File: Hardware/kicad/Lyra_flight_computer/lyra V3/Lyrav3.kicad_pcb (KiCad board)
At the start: 4 copper layers, 25 x 55 mm, 80 parts, among them J2 Screw_Terminal_01x06, J3 Conn_01x02, J4 Conn_01x02, J5 Conn_01x03, J6 Conn_01x06, J7 USB_B_Micro, J8 Conn_01x04, J9 Screw_Terminal_01x06, Q1 AO3401A, Q2 AO3400A, Q3 AO3400A, Q4 AO3400A, Q5 AO3400A, U1 AZ1117-3.3, U2 BMI088, U3 BMP388, U4 ADXL375BCCZ-RL7, U6 ADS1015IDGS, U8 RP2040, U9 W25Q128JVS, X1 S3D12.288000B20F30T

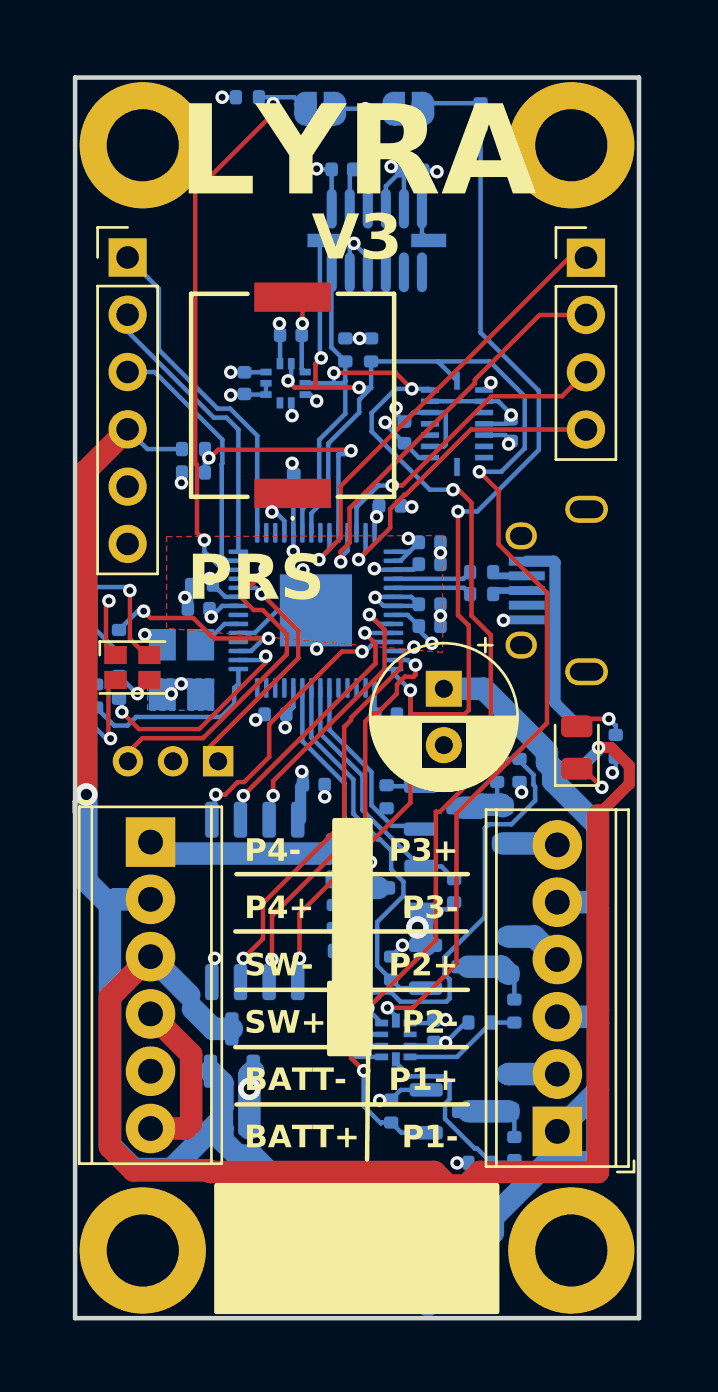
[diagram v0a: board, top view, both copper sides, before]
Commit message: add gps module init
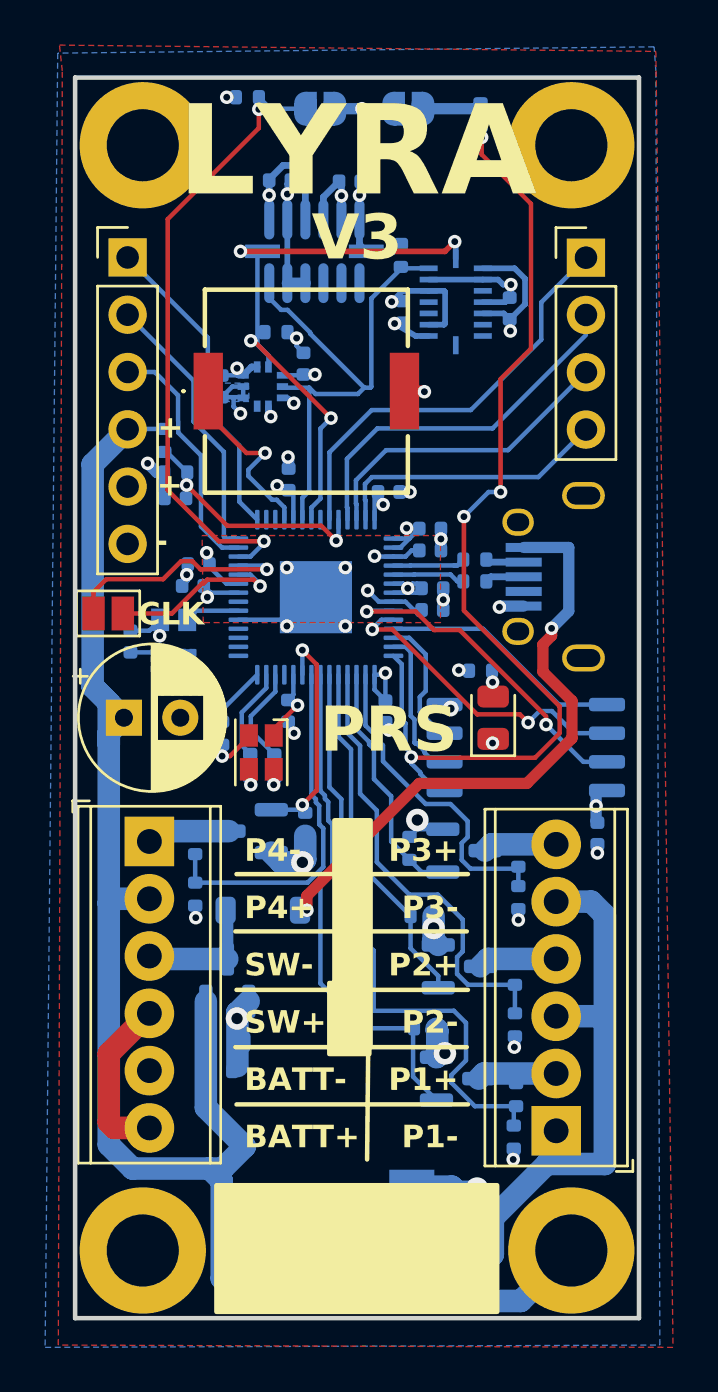
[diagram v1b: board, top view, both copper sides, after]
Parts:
- removed C15: 100n, Capacitor_SMD:C_0402_1005Metric
- removed J5: Conn_01x03, Connector_PinHeader_2.00mm:PinHeader_1x03_P2.00mm_Vertical
- removed R19, R20, R8, R9: 1R, Resistor_SMD:R_0603_1608Metric
- removed U1: AZ1117-3.3, Package_TO_SOT_SMD:SOT-223
- removed U6: ADS1015IDGS, easyeda2kicad:X2QFN-10_L2.0-W1.5-P0.50-BL
- removed X1: S3D12.288000B20F30T, easyeda2kicad:OSC-SMD_4P-L3.2-W2.5-BL_SIT8008BI
- added C13: 100n, Capacitor_SMD:C_0402_1005Metric, B.Cu at (186.1, 89.0)
- added C3: 100n, Capacitor_SMD:C_0402_1005Metric, B.Cu at (188.0, 82.7)
- added J1: Conn_01x02, Jumper:SolderJumper-2_P1.3mm_Open_Pad1.0x1.5mm, F.Cu at (185.1, 87.8)
- added U5: AMS1117-3.3, Package_TO_SOT_SMD:SOT-223-3_TabPin2, B.Cu at (195.4, 115.5)
- added X2: SX1M12.000M10F30TNN, easyeda2kicad:OSC-SMD_4P-L2.0-W1.6-BL, B.Cu at (188.0, 89.0)
- C5, C6, C7: footprint Capacitor_SMD:C_0402_1005Metric -> Capacitor_SMD:C_0603_1608Metric
- D1: footprint Diode_SMD:D_SOD-323 -> Diode_SMD:D_SOD-123
- moved D1 15.7 mm to (191.9, 100.9), turned to 0 degrees
- moved C9 14.2 mm to (185.8, 92.4), turned to 0 degrees
- moved U9 13.8 mm to (203.6, 93.7), turned to 0 degrees
- moved C27 12.8 mm to (206.8, 97.5), turned to -90 degrees
- moved R28 8.82 mm to (192.4, 94.5)
- moved R27 7.23 mm to (193.8, 97.1)
- moved R25 7.11 mm to (188.9, 100.2), turned to -90 degrees
- moved Q5 7.09 mm to (191.4, 97.4)
- moved R23 6.97 mm to (188.9, 97.9)
- moved R3 6.87 mm to (201.6, 90.3), turned to 180 degrees
- moved D4 6.84 mm to (191.9, 93.9), turned to -90 degrees
- moved R22 6.77 mm to (191.4, 94.5), turned to -90 degrees
- moved R2 5.83 mm to (190.1, 93.1), turned to -90 degrees
- moved R13 5.64 mm to (203.3, 100.4)
- moved C2 5.39 mm to (202.9, 74.3)
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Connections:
- Q2 pad 3: Net-(Q2-D) -> /P2-
- Q3 pad 3: Net-(Q3-D) -> /P1-
- Q4 pad 3: Net-(Q4-D) -> /P3-
- Q5 pad 3: Net-(Q5-D) -> /P4-
- R10 pad 1: Net-(Q3-D) -> /P1-
- R11 pad 1: Net-(Q4-D) -> /P3-
- R21 pad 1: Net-(Q2-D) -> /P2-
- R23 pad 1: Net-(Q5-D) -> /P4-
- U8 pad 12: unconnected-(U8-GPIO9-Pad12) -> /LEDBLUE
- U8 pad 13: unconnected-(U8-GPIO10-Pad13) -> /LEDGREEN
- U8 pad 14: unconnected-(U8-GPIO11-Pad14) -> /LEDRED
- U8 pad 15: /LEDRED -> unconnected-(U8-GPIO12-Pad15)
- U8 pad 16: /LEDGREEN -> unconnected-(U8-GPIO13-Pad16)
- U8 pad 17: /LEDBLUE -> unconnected-(U8-GPIO14-Pad17)
- U8 pad 2: unconnected-(U8-GPIO0-Pad2) -> /P3 CONT 
- U8 pad 3: unconnected-(U8-GPIO1-Pad3) -> /P3 EN 
- U8 pad 4: unconnected-(U8-GPIO2-Pad4) -> /P2 CONT 
- U8 pad 5: unconnected-(U8-GPIO3-Pad5) -> /P2 EN 
- U8 pad 6: /P3 EN  -> /P1 CONT 
- U8 pad 7: /P4 EN  -> /P1 EN 
- U8 pad 8: /P2 EN  -> /P4 CONT 
- U8 pad 9: /P1 EN  -> /P4 EN 
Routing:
- net +12V: track 58.1 -> 5.52 mm, vias 1 -> 0
- net /I2C1 SCL: track 62.8 -> 25.7 mm, vias 5 -> 4
- net /I2C1 SDA: track 54.3 -> 23.8 mm, vias 4 -> 0
- net /P1 CONT : track 8.52 -> 27.2 mm
- net VBUS: track 8.86 -> 26.8 mm, vias 0 -> 2
- net /P2 CONT : track 5.25 -> 20.3 mm
- net /QSPI_SD2: track 19.0 -> 5.60 mm, vias 2 -> 0
- net /QSPI_SD1: track 18.1 -> 6.19 mm, vias 2 -> 0
- net /P4 CONT : track 7.24 -> 16.0 mm
- net +12P: track 103.3 -> 95.1 mm, vias 1 -> 0
- net Net-(D4-BK): track 8.25 -> 0.34 mm
- net /P3 CONT : track 22.2 -> 14.4 mm
- net /BUZZER: track 1.25 -> 8.31 mm
- net /LEDGREEN: track 10.1 -> 4.11 mm, vias 2 -> 0
- net GND: track 65.5 -> 59.6 mm, vias 35 -> 36
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- added copper zone on B.Cu, net (none)
- added copper zone on F.Cu, net (none)
- added copper zone on B.Cu, net GND
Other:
- board text added: "+"
- board text added: "-"
- board text added: "CLK"
